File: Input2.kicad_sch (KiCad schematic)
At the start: 12 parts, among them J601 Power Input

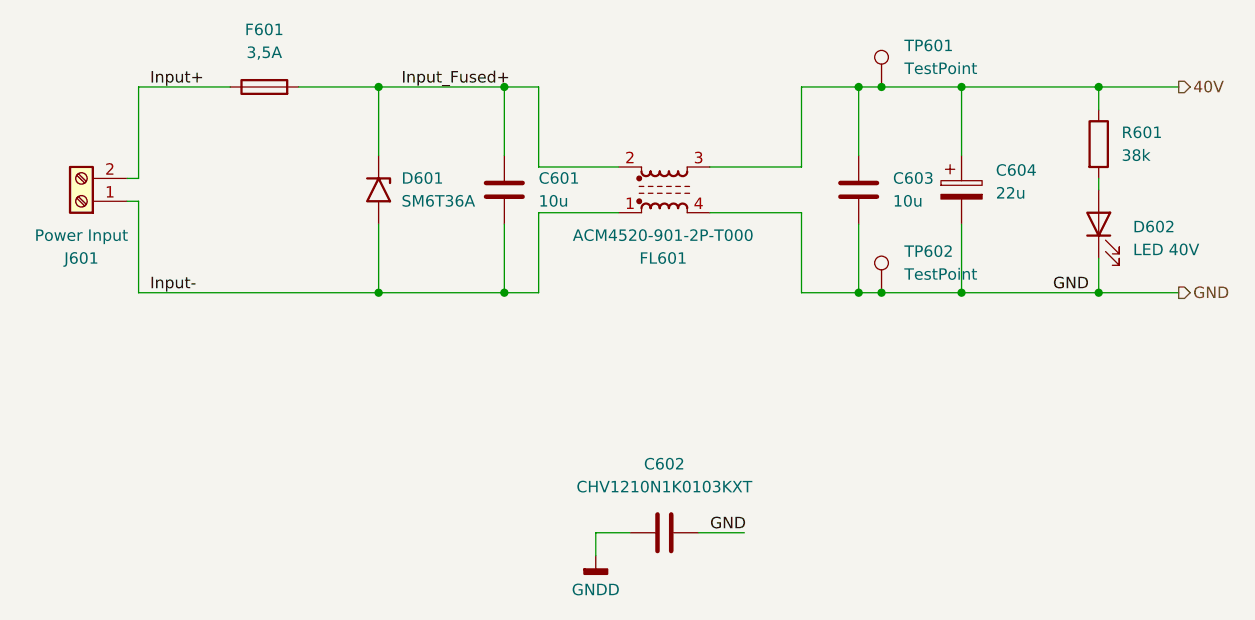
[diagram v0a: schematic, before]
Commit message: added Ch2 and removed global power flags
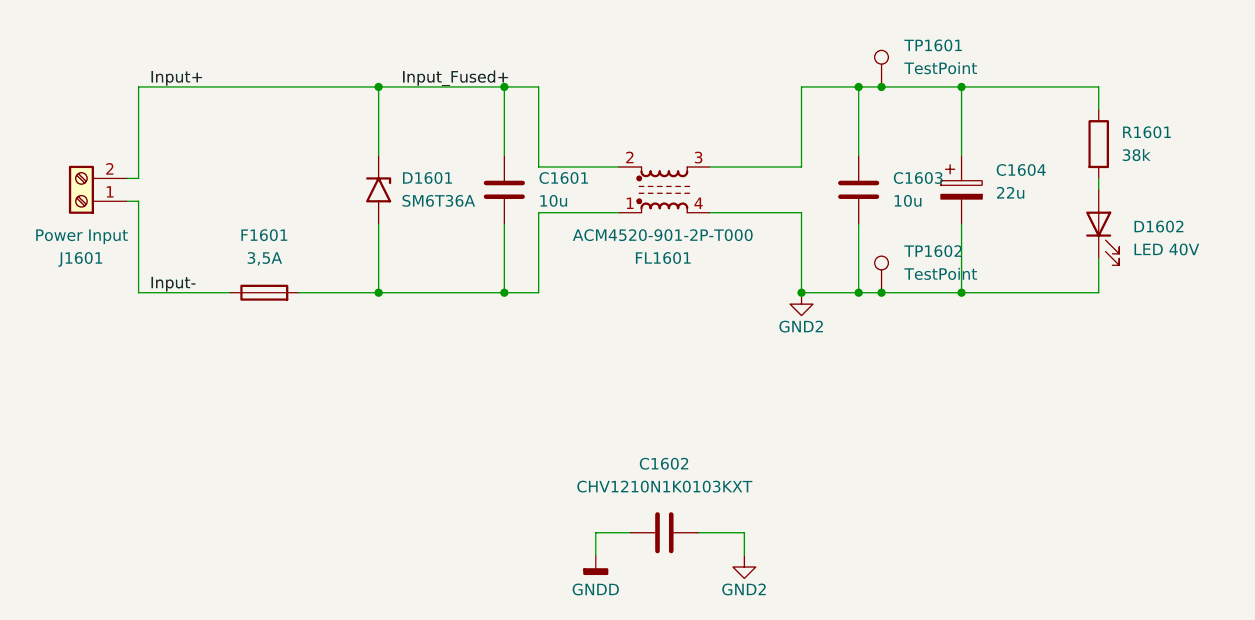
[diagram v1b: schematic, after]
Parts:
- removed C601, C603: 10u, Capacitor_SMD:C_1206_3216Metric, symbol Device:C
- removed C602: CHV1210N1K0103KXT, Capacitor_SMD:C_1210_3225Metric, symbol Device:C
- removed C604: 22u, Capacitor_SMD:CP_Elec_8x10.5, symbol Device:C_Polarized
- removed D601: SM6T36A, Diode_SMD:D_SMB, symbol Diode:SM6T36A
- removed D602: LED 40V, LED_SMD:LED_0603_1608Metric, symbol Device:LED
- removed F601: 3,5A, Fuse:Fuse_1206_3216Metric, symbol Device:Fuse
- removed FL601: ACM4520-901-2P-T000, LibEigen:ACM4520_TDK, symbol Filter:Choke_CommonMode_FerriteCore_1423
- removed J601: Power Input, Connector_Phoenix_MC:PhoenixContact_MCV_1,5_2-G-3.81_1x02_P3.81mm_Vertical, symbol Connector:Screw_Terminal_01x02
- removed R601: 38k, Resistor_SMD:R_0603_1608Metric, symbol Device:R
- removed TP601, TP602: TestPoint, LibEigen:SMD Test Point PCWCTE, symbol Connector:TestPoint
- added C1601, C1603: 10u, Capacitor_SMD:C_1206_3216Metric, symbol Device:C
- added C1602: CHV1210N1K0103KXT, Capacitor_SMD:C_1210_3225Metric, symbol Device:C
- added C1604: 22u, Capacitor_SMD:CP_Elec_8x10.5, symbol Device:C_Polarized
- added D1601: SM6T36A, Diode_SMD:D_SMB, symbol Diode:SM6T36A
- added D1602: LED 40V, LED_SMD:LED_0603_1608Metric, symbol Device:LED
- added F1601: 3,5A, Fuse:Fuse_1206_3216Metric, symbol Device:Fuse
- added FL1601: ACM4520-901-2P-T000, LibEigen:ACM4520_TDK, symbol Filter:Choke_CommonMode_FerriteCore_1423
- added J1601: Power Input, Connector_Phoenix_MC:PhoenixContact_MCV_1,5_2-G-3.81_1x02_P3.81mm_Vertical, symbol Connector:Screw_Terminal_01x02
- added R1601: 38k, Resistor_SMD:R_0603_1608Metric, symbol Device:R
- added TP1601, TP1602: TestPoint, LibEigen:SMD Test Point PCWCTE, symbol Connector:TestPoint
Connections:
- net GNDD: now also C1602.1
- net Input+: now also C1601.1, D1601.1 (A1), FL1601.2, J1601.2 (Pin_2)
- net Input-: now also F1601.1, J1601.1 (Pin_1)
- new net: C1603.1, C1604.1, FL1601.3, R1601.1, TP1601.1
- new net: C1601.2, D1601.2 (A2), F1601.2, FL1601.1
- new net: D1602.2 (A), R1601.2
- new net GND2: C1602.2, C1603.2, C1604.2, D1602.1 (K), FL1601.4, TP1602.1
